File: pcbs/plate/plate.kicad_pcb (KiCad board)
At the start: 2 copper layers, 133.4 x 91.4 mm, 0 parts

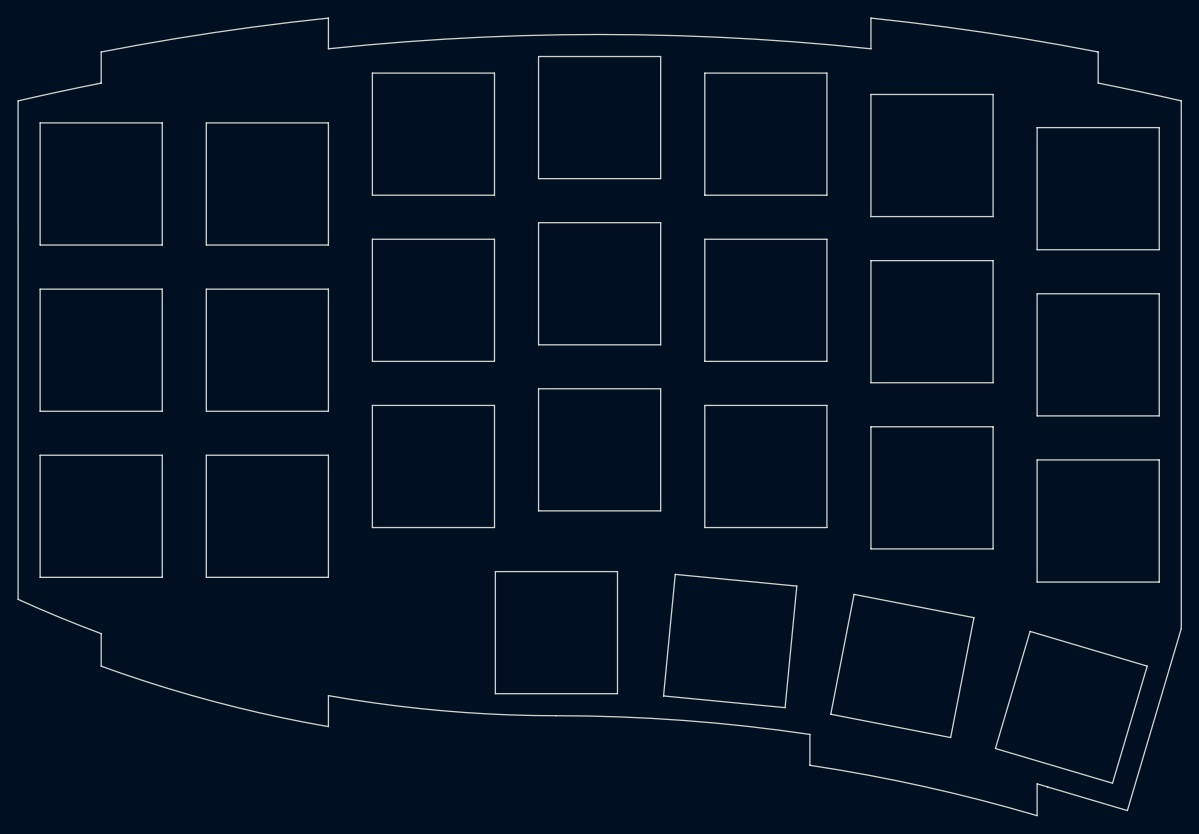
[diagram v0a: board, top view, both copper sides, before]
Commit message: Drop the order number marker and thicken the plate outline
JLCPCB's order form now offers removing the order number but not
placing it, so remove the JLCJLCJLCJLC marker from the plate. Draw the
outline and switch cutouts 0.15 mm wide instead of 0.05 mm: the thin
lines dropped out of JLCPCB's preview, which made the cutouts look
missing. Milling follows the line centers, so the shapes are unchanged.

Co-Authored-By: Claude Opus 5.5 <noreply@anthropic.com>
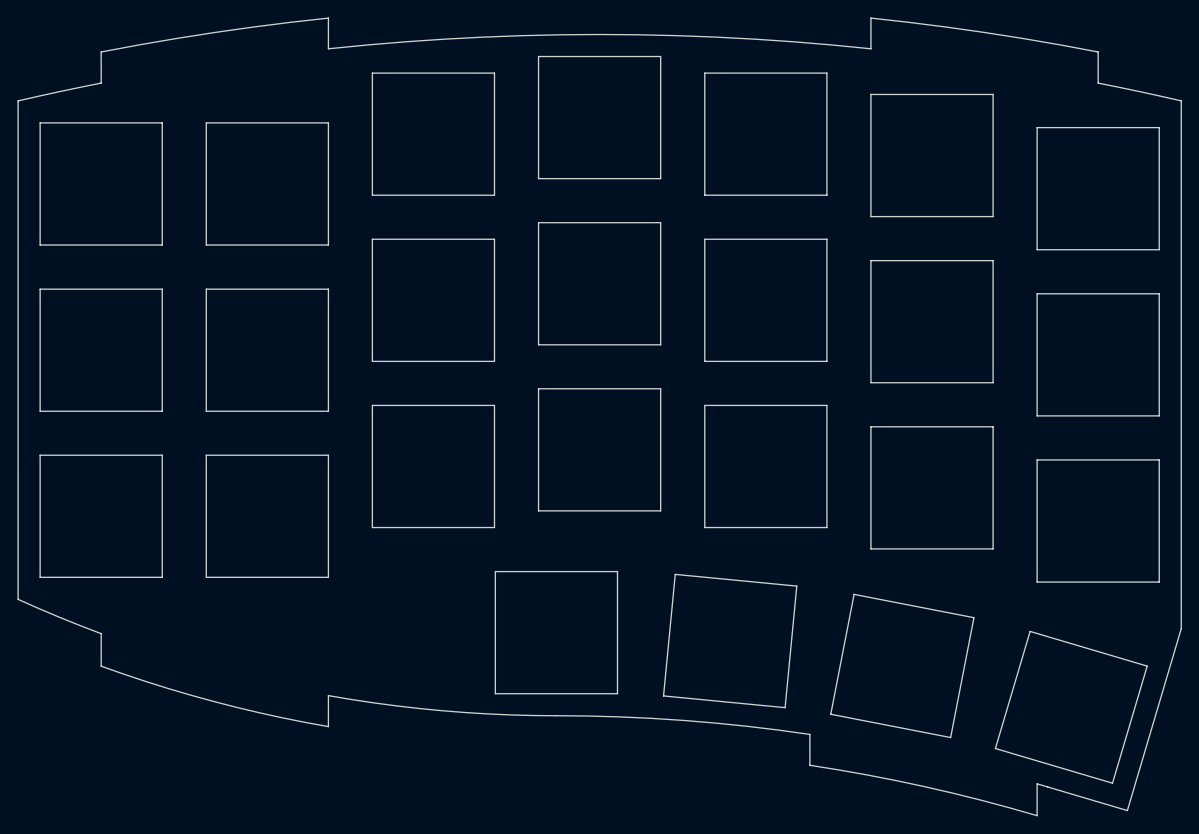
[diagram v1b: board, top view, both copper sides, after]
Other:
- board text removed: "JLCJLCJLCJLC"
